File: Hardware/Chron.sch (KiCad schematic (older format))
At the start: 2 parts

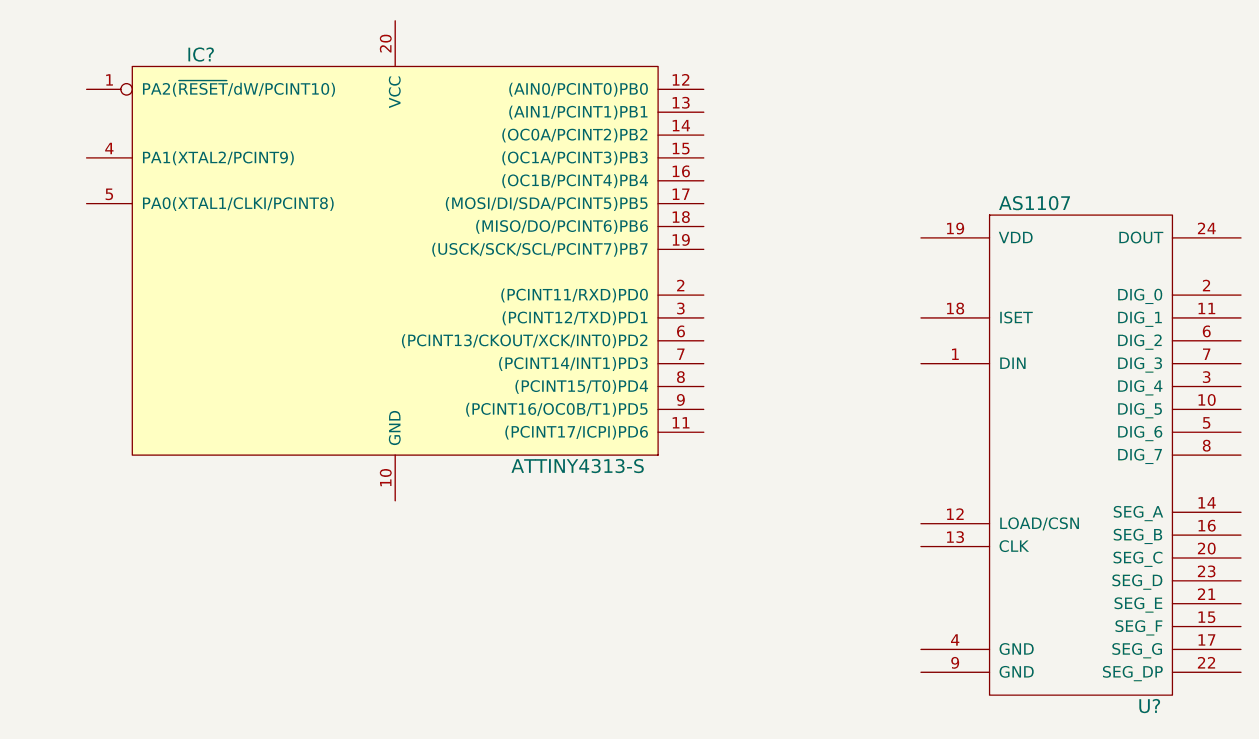
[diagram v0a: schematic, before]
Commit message: Determined the specifications for the project
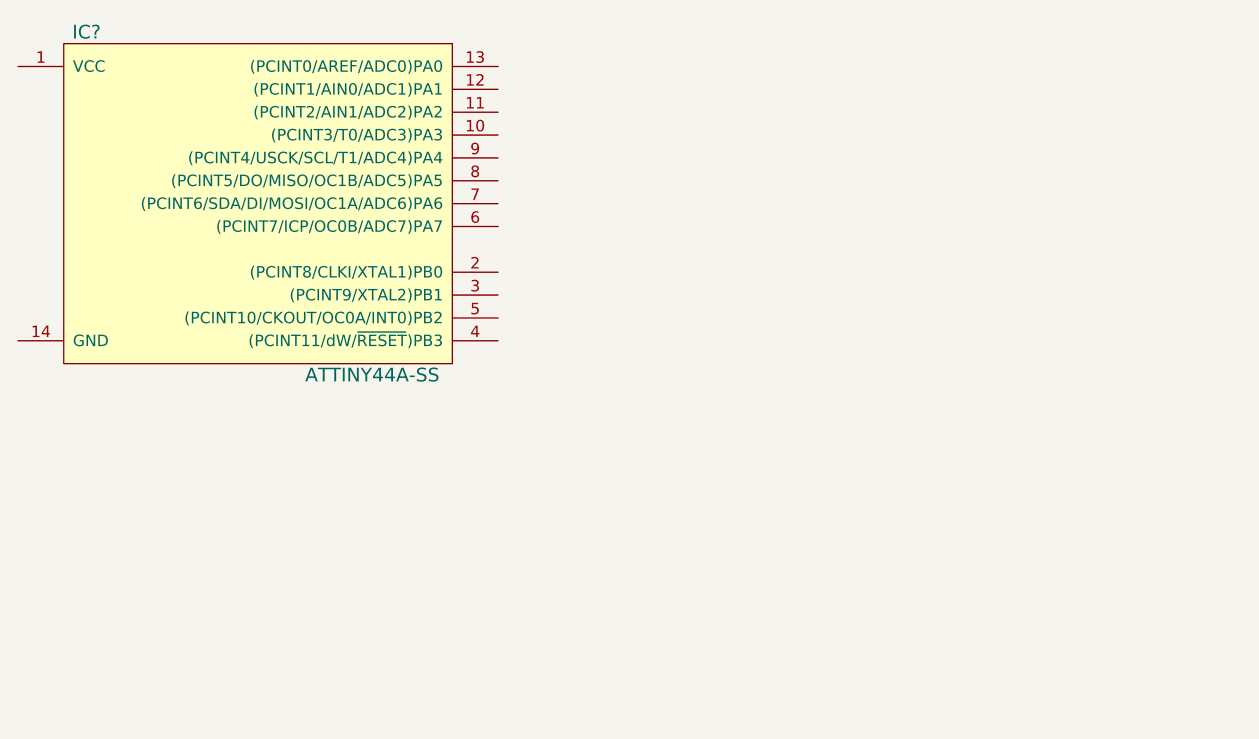
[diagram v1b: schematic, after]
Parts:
- removed IC?: ATTINY4313-S, SO20, symbol ATTINY4313-S
- removed U?: AS1107, symbol AS1107
- added IC?: ATTINY44A-SS, SO14, symbol ATTINY44A-SS
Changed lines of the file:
@@
-EESchema Schematic File Version 2  date 5/20/2012 12:47:53 AM
+EESchema Schematic File Version 2  date 7/3/2012 7:00:54 PM
 LIBS:power
 LIBS:device
@@
 Sheet 1 1
 Title "Chron - A digitally controlled analog clock"
-Date "20 may 2012"
+Date "3 jul 2012"
 Rev "1.0"
 Comp "Projects and Stuff LLC"
@@
 $EndDescr
 $Comp
-L AS1107 U?
-U 1 1 4FB87764
-P 6300 3800
-F 0 "U?" H 6600 2700 60  0000 C CNN
-F 1 "AS1107" H 6100 4900 60  0000 C CNN
-	1    6300 3800
+L ATTINY44A-SS IC?
+U 1 1 4FF378A8
+P 2700 2700
+F 0 "IC?" H 1950 3450 60  0000 C CNN
+F 1 "ATTINY44A-SS" H 3200 1950 60  0000 C CNN
+F 2 "SO14" H 2000 1950 60  0001 C CNN
+	1    2700 2700
 	1    0    0    -1
 $EndComp
-$Comp
-L ATTINY4313-S IC?
-U 1 1 4FB87690
-P 3300 3000
-F 0 "IC?" H 2450 3950 60  0000 C CNN
-F 1 "ATTINY4313-S" H 4100 2150 60  0000 C CNN
-F 2 "SO20" H 2300 2150 60  0001 C CNN
-	1    3300 3000
-	1    0    0    -1
-$EndComp
